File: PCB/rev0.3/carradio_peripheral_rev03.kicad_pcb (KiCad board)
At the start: 4 copper layers, 109 x 92 mm, 258 parts, among them J1 ISO 10487 A (via pigtail), J10 Expansion, J11 SMA GNSS antenna, J12 Display buttons, J13 HDMI in (from VIM3), J14 Display FPC 40P 0.5mm, J17 RTL-SDR (internal), J18 VIM3 VIN (JST-XH 2P), J19 External USB 1, J2 VIM3 40-pin via 2x20 IDC ribb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, J20 External USB 2, J21 Expansion 2, J22 SWD, J5 VIM3 POWER key lead, J7 BH1750 light sensor, J8 ISO 10487 C1 (via pigtail), Q1 AO3400A, Q10 P-MOSFET -40V, Q11 CSD18543Q3A, Q12 CSD18543Q3A, Q2 P-MOSFET -60V, Q3 2N7002, SW1 BOOTSEL, SW2 RESET, U1 TPS560430XDBVR, U10 PCM5102APWR, U11 PCM5102APWR, U12 TPS55288RPMR, U13 CH334R, U14 CH334R, U15 LMR33630ADDA, U16 TPS2561DRCR, U17 USBLC6-2SC6, U18 USBLC6-2SC6, U19 AP2112K-3.3, U2 EL817S1(C), U20 RP2350B, U21 W25Q128JVS, U3 EL817S1(C), U4 EL817S1(C), U5 EL817S1(C), U6 LP5907MFX-3.3, U7 NEO-M9N-00B, U8 LP5907MFX-3.3, U9 LP5907MFX-3.3, Y1 12MHz, Y2 12MHz, Y3 12MHz

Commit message: PCB rev 0.3: fully routed board with corner mounting tabs
The board now has every connection routed. KiCad DRC reports 0 unconnected
items and no copper errors; only silkscreen warnings remain.

- TPS55288 stage re-placed around U12 with locked power copper zones.
- Signal vias are 0.45/0.2 mm; VSYS_IN and +5V_SYS use 0.6/0.3 mm.
- R69 (ILIM) and TH1 swapped so R69 sits next to U12 pin 17.
- Four 8 x 9 mm corner tabs with plated M3 holes on GND; the board is
  now 125 x 92 mm overall.
- Layout scripts and hand-edit files added under layout/ (see README).

Co-Authored-By: Claude Opus 5.5 (1M context) <noreply@anthropic.com>
Claude-Session: https://claude.ai/code/session_01C8m2AkFwQrNE2yN9Ymgjwu
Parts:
- added H1: M3, MountingHole:MountingHole_3.2mm_M3_Pad_Via, F.Cu at (-4.00, 4.50)
- added H2: M3, MountingHole:MountingHole_3.2mm_M3_Pad_Via, F.Cu at (-4.00, 87.5)
- added H3: M3, MountingHole:MountingHole_3.2mm_M3_Pad_Via, F.Cu at (113.0, 4.50)
- added H4: M3, MountingHole:MountingHole_3.2mm_M3_Pad_Via, F.Cu at (113.0, 87.5)
- moved J21 58.2 mm to (60.3, 37.8)
- moved J10 49.0 mm to (64.6, 37.8), turned to 0 degrees
- moved SW1 41.1 mm to (71.0, 41.5)
- moved SW2 41.1 mm to (71.0, 48.5)
- moved R81 40.2 mm to (69.8, 37.0)
- moved F2 35.6 mm to (47.0, 81.8), turned to 0 degrees
- moved R1 33.1 mm to (4.75, 45.8)
- moved D12 30.3 mm to (3.00, 76.0)
- moved R72 28.1 mm to (39.8, 54.8), turned to 90 degrees
- moved R40 24.4 mm to (2.00, 29.8)
- moved R68 21.7 mm to (46.8, 65.8), turned to 90 degrees
- moved C64 21.5 mm to (20.0, 59.0), turned to 0 degrees
- moved R89 21.2 mm to (55.8, 19.2)
- moved Q1 20.4 mm to (14.5, 79.0)
- moved R33 19.8 mm to (57.2, 36.5), turned to 90 degrees
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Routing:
- net /+3V3_MCU: track 0.00 -> 326.0 mm, vias 0 -> 12
- net /+5V_SYS: track 0.00 -> 159.6 mm, vias 0 -> 31
- net /LUX_SCL: track 0.00 -> 149.0 mm, vias 0 -> 4
- net /LUX_SDA: track 0.00 -> 146.3 mm, vias 0 -> 7
- net /AMP_REM: track 0.00 -> 142.2 mm, vias 0 -> 5
- net /+5V_AON: track 0.00 -> 140.4 mm, vias 0 -> 6
- net /VIM3_5V: track 0.00 -> 138.1 mm, vias 0 -> 3
- net /MCU_RUN: track 0.00 -> 134.0 mm, vias 0 -> 4
- net /MCU_BTN_VOLUP: track 0.00 -> 120.9 mm, vias 0 -> 5
- net /I2S_BCLK: track 0.00 -> 111.0 mm, vias 0 -> 4
- net /VSYS_IN: track 0.00 -> 110.3 mm, vias 0 -> 8
- net /VBAT_P: track 0.00 -> 110.2 mm, vias 0 -> 5
- net /DAC_XSMT: track 0.00 -> 108.5 mm, vias 0 -> 8
- net /MCU_USBP_PG: track 0.00 -> 105.6 mm, vias 0 -> 4
- net /MCU_BL_EN: track 0.00 -> 104.7 mm, vias 0 -> 3
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- added copper zone on B.Cu, net /+5V_SYS
- added copper zone on F.Cu, net /+5V_SYS
- added copper zone on F.Cu, net /BATT_F2
- added copper zone on B.Cu, net /BATT_RAW
- added copper zone on F.Cu, net /BATT_RAW
- added copper zone on F.Cu, net /BB_SW1
- added copper zone on F.Cu, net /BB_SW2
- added copper zone on F.Cu, net /BB_VOUT
- added copper zone on F.Cu, net /VSYS_IN
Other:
- board size 109 x 92 mm -> 125 x 92 mm

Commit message: PCB rev 0.3: rework TPS55288 area per TI layout guide (SLVAER0C)
- Schematic: net ties NT1/NT2 give ISP/ISN Kelvin taps at R74; NT3 joins
  a new analog ground (BB_AGND: U12 pins 7/10, R67-R70, C54, C55) to GND
  at the VCC cap. BOM unchanged.
- Layout: VCC cap at pin 19, BOOT caps on F.Cu without vias, control
  parts in a row beside U12 on an AGND pour, ISP/ISN routed as a pair.
  Displaced nets re-routed. DRC: 0 unconnected, no copper or courtyard
  errors.
- TPS55288_LAYOUT_REVIEW.md lists what changed and what was left.

Co-Authored-By: Claude Opus 5.5 (1M context) <noreply@anthropic.com>
Claude-Session: https://claude.ai/code/session_01C8m2AkFwQrNE2yN9Ymgjwu
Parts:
- added NT1: NetTie, NetTie:NetTie-2_SMD_Pad0.5mm, F.Cu at (42.5, 70.5)
- added NT2: NetTie, NetTie:NetTie-2_SMD_Pad0.5mm, F.Cu at (41.0, 74.5)
- added NT3: NetTie, NetTie:NetTie-2_SMD_Pad0.5mm, F.Cu at (39.9, 63.6)
- moved C54 15.2 mm to (42.0, 61.1)
- moved R68 13.7 mm to (33.9, 70.5), turned to -90 degrees
- moved C103 6.59 mm to (43.9, 57.5), turned to 90 degrees
- moved R71 6.15 mm to (42.0, 64.2)
- moved C53 4.81 mm to (38.9, 64.4)
- moved C55 4.54 mm to (40.4, 64.2)
- moved R67 3.04 mm to (46.6, 64.2)
- moved R70 2.98 mm to (45.0, 64.2)
- moved R69 2.48 mm to (43.5, 64.2), turned to 90 degrees
- moved C52 1.63 mm to (37.3, 63.6)
- moved C56 0.40 mm to (36.6, 74.9)
- moved C57 0.40 mm to (36.6, 77.0)
- moved C58 0.40 mm to (36.6, 70.7)
- moved C59 0.40 mm to (36.6, 72.8)
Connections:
- C54 pad 2: GND -> /BB_AGND
- C55 pad 2: GND -> /BB_AGND
- R67 pad 2: GND -> /BB_AGND
- R68 pad 2: GND -> /BB_AGND
- R69 pad 2: GND -> /BB_AGND
- R70 pad 2: GND -> /BB_AGND
- U12 pad 10: GND -> /BB_AGND
- U12 pad 12: /BB_VOUT -> /BB_ISP
- U12 pad 13: /+5V_SYS -> /BB_ISN
- U12 pad 7: GND -> /BB_AGND
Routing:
- net /BB_FSW: track 30.7 -> 1.27 mm, vias 4 -> 0
- net /BB_COMP_RC: track 23.7 -> 1.45 mm, vias 2 -> 0
- net /RPP_G: track 28.3 -> 44.2 mm
- net /BB_AGND: track 0.00 -> 13.8 mm, vias 0 -> 3
- net /BB_COMP: track 15.9 -> 4.60 mm, vias 2 -> 0
- net GND: track 243.9 -> 235.4 mm, vias 192 -> 187
- net /BB_ISP: track 0.00 -> 8.52 mm, vias 0 -> 2
- net /BB_ISN: track 0.00 -> 6.89 mm, vias 0 -> 2
- net /+5V_SYS: track 159.6 -> 152.8 mm, vias 31 -> 29
- net /MCU_TEMP_ADC: track 55.8 -> 49.4 mm, vias 4 -> 3
- net /BB_VCC: track 6.19 -> 0.87 mm
- net /BB_BOOT2: track 4.68 -> 0.32 mm, vias 2 -> 0
- net /+5V_AON: track 140.4 -> 144.6 mm, vias 6 -> 9
- net /BB_CDC: track 12.5 -> 8.59 mm
- net /MCU_BTN_VOLDN: track 93.3 -> 90.0 mm
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- added copper zone on F.Cu, net /BB_AGND

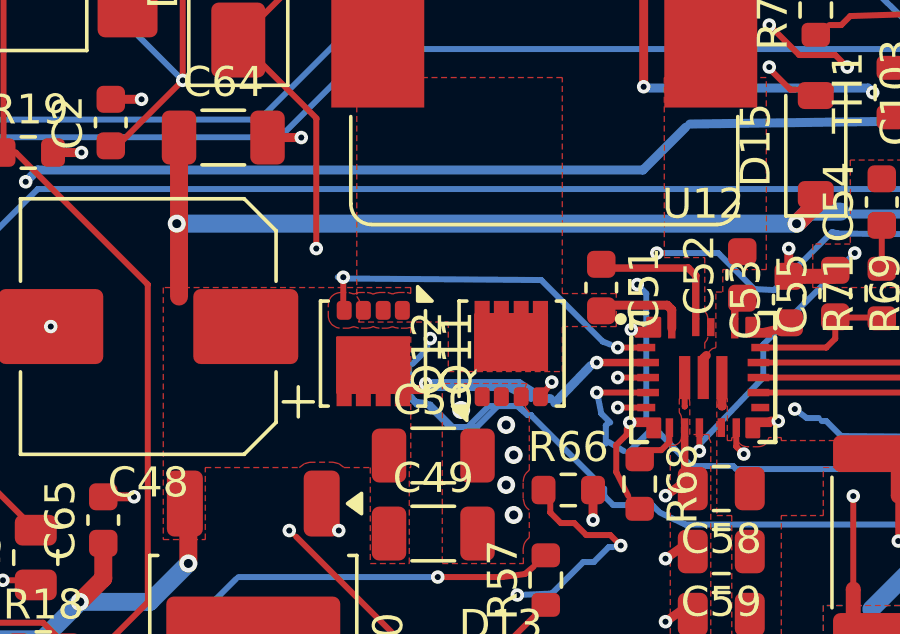
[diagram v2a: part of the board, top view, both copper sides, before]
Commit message: PCB rev 0.3: TPS55288 gate resistors and SW1 snubber
Adds R97/R98 (0402, fitted as 0 ohm) in series with the DR1H and DR1L
gates and an RC snubber C104 (1nF) + R99 (2.2 ohm 0805) from SW1 to GND,
the two items the TI layout review left open. Schematic, BOM and board
updated; DRC 0 unconnected, no copper or courtyard errors.

Co-Authored-By: Claude Opus 5.5 (1M context) <noreply@anthropic.com>
Claude-Session: https://claude.ai/code/session_01C8m2AkFwQrNE2yN9Ymgjwu
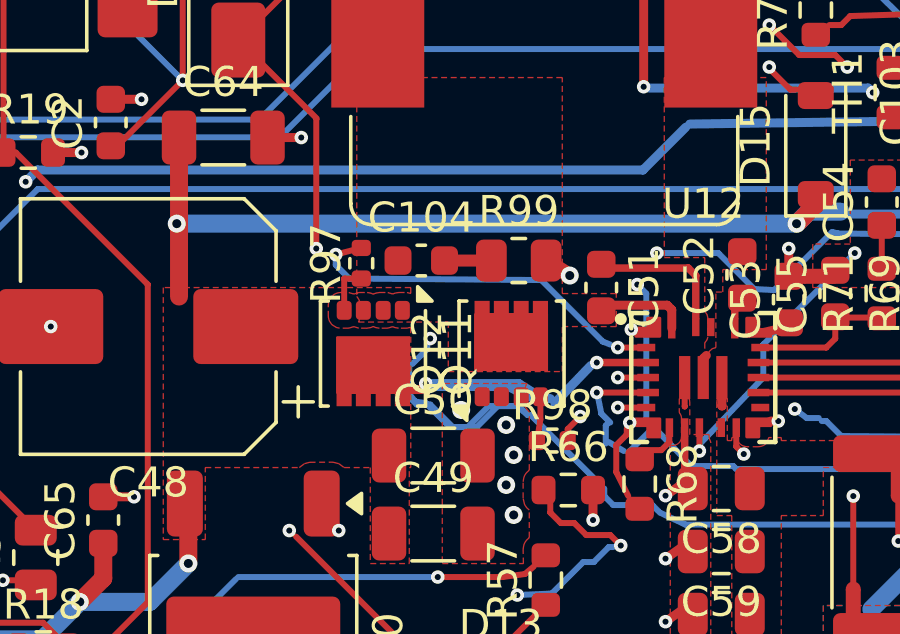
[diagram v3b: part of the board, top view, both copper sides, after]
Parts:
- added C104: 1nF, Capacitor_SMD:C_0603_1608Metric, F.Cu at (26.6, 63.1)
- added R97: 0Ω, Resistor_SMD:R_0402_1005Metric, F.Cu at (24.6, 63.2)
- added R98: 0Ω, Resistor_SMD:R_0402_1005Metric, F.Cu at (31.0, 69.1)
- added R99: 2.2Ω 0805, Resistor_SMD:R_0805_2012Metric, F.Cu at (29.9, 63.1)
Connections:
- Q11 pad 4: /BB_DR1H -> /BB_DR1H_G
- Q12 pad 4: /BB_DR1L -> /BB_DR1L_G
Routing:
- net /BB_DR1H_G: track 0.00 -> 1.63 mm
- net /BB_SNUB: track 0.00 -> 1.56 mm
- net /BB_DR1L_G: track 0.00 -> 1.47 mm
- net /BB_DR1L: track 4.52 -> 5.65 mm
- net GND: track 235.4 -> 236.3 mm, vias 187 -> 188
- net /BB_DR1H: track 11.8 -> 12.4 mm
